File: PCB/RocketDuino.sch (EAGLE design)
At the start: 41 parts, among them J1 FTDI, Y1 16MHZ

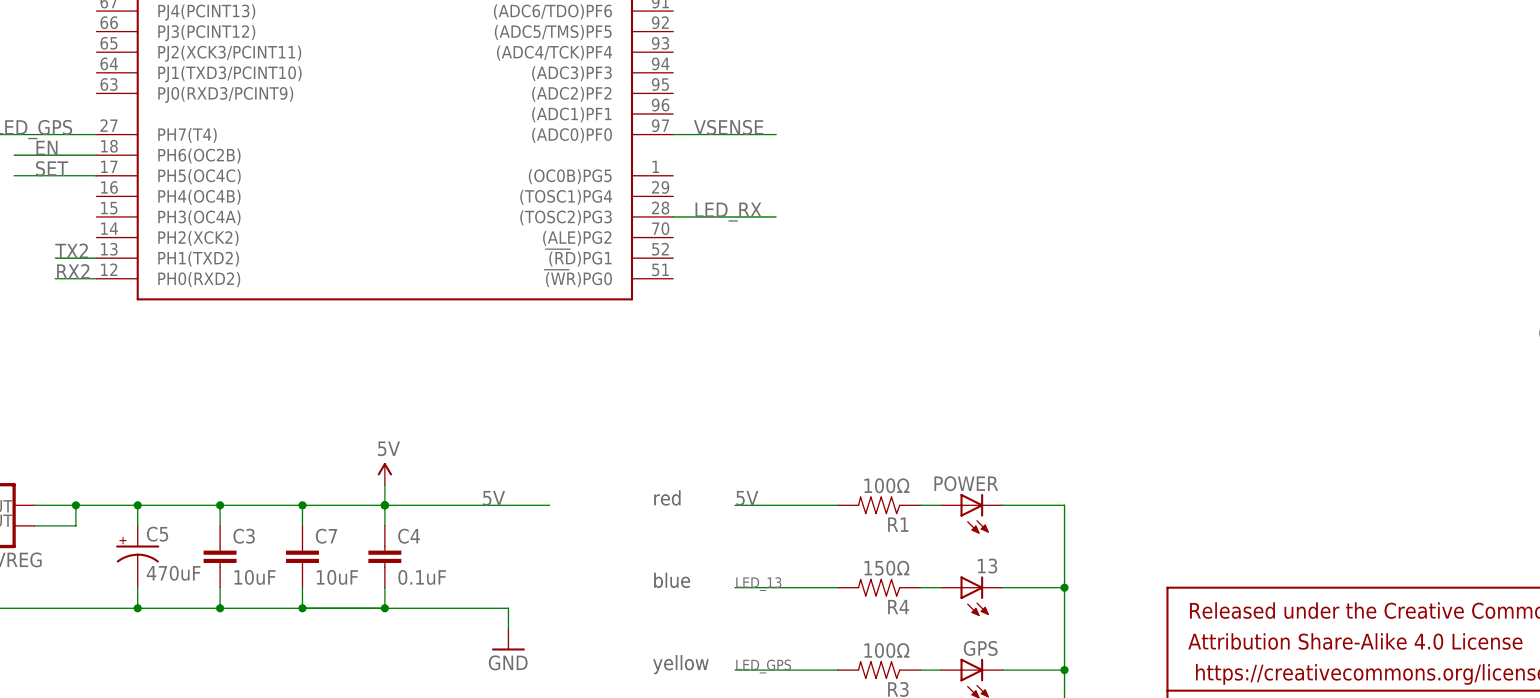
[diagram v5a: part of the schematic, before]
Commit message: Made C4 Explosive
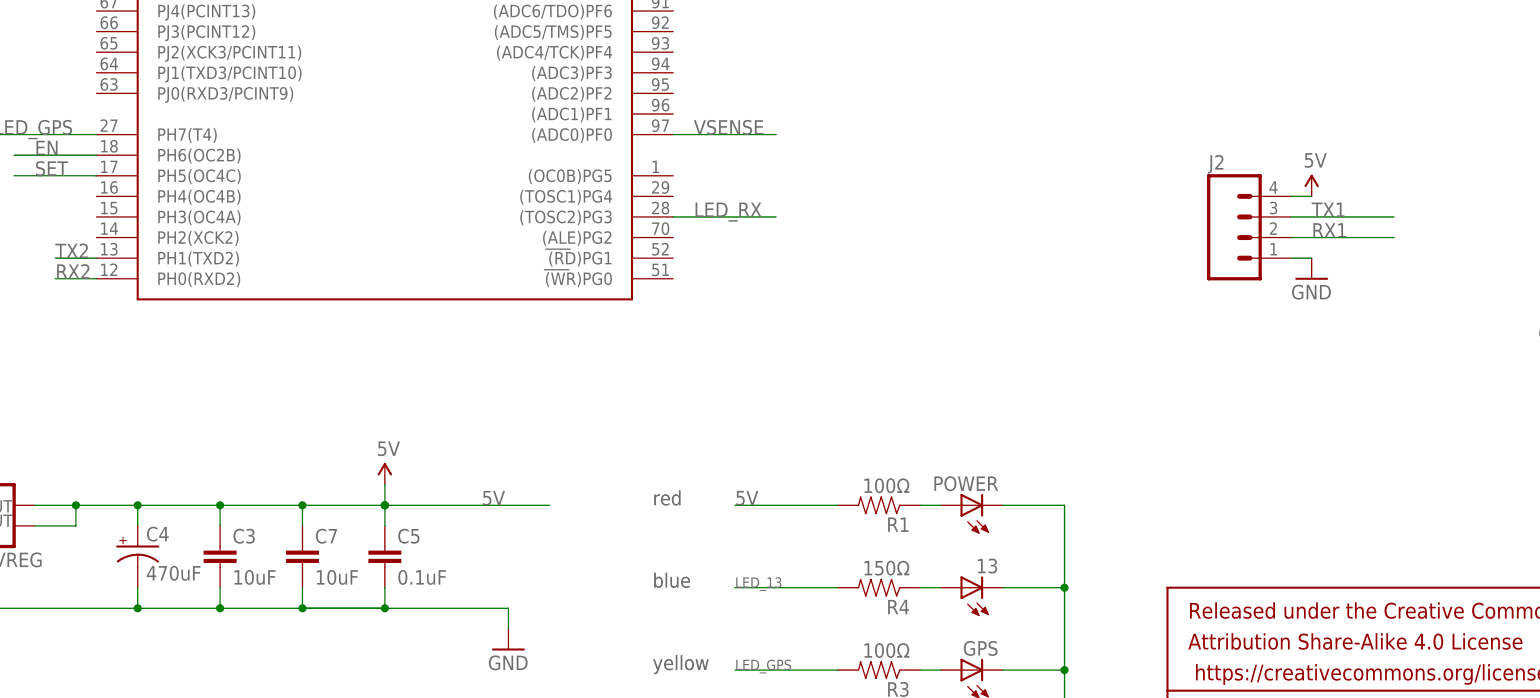
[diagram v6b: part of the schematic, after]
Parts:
- added J2: (no value), SparkFun-Connectors:M04POLAR
- C4: value 0.1uF -> 470uF; device SparkFun-Capacitors:CAP1206 -> SparkFun-Capacitors:CAP_POLPTH1
- C5: value 470uF -> 0.1uF; device SparkFun-Capacitors:CAP_POLPTH1 -> SparkFun-Capacitors:CAP1206
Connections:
- net 5V: now also C4.+, C5.1, J2.4; no longer C4.1, C5.+
- net GND: now also C4.-, C5.2, J2.1; no longer C4.2, C5.-
- net RX1: now also J2.2
- net TX1: now also J2.3
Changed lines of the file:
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@@
 <part name="SUPPLY5" library="SparkFun-Aesthetics" deviceset="5V" device=""/>
 <part name="C1" library="SparkFun-Capacitors" deviceset="CAP" device="1206" value="0.1uF"/>
-<part name="C4" library="SparkFun-Capacitors" deviceset="CAP" device="1206" value="0.1uF"/>
+<part name="C5" library="SparkFun-Capacitors" deviceset="CAP" device="1206" value="0.1uF"/>
 <part name="C2" library="SparkFun-Capacitors" deviceset="CAP" device="1206" value="10uF"/>
 <part name="C3" library="SparkFun-Capacitors" deviceset="CAP" device="1206" value="10uF"/>
@@
 <part name="CH_2" library="SparkFun-Connectors" deviceset="M02" device="LOCK_LONGPADS"/>
 <part name="VREG" library="SparkFun-PowerIC" deviceset="V_REG_LM1117" device="SOT223"/>
-<part name="C5" library="SparkFun-Capacitors" deviceset="CAP_POL" device="PTH1" value="470uF"/>
+<part name="C4" library="SparkFun-Capacitors" deviceset="CAP_POL" device="PTH1" value="470uF"/>
 <part name="Y1" library="SparkFun-FreqCtrl" deviceset="RESONATOR" device="16MHZ" value="16MHZ"/>
 <part name="R9" library="SparkFun-Resistors" deviceset="RESISTOR" device="1206" value="1MΩ"/>
@@
 <part name="MAIN" library="SparkFun-Connectors" deviceset="M02" device="LOCK_LONGPADS"/>
 <part name="C10" library="SparkFun-Capacitors" deviceset="CAP" device="1206" value="10uF"/>
+<part name="J2" library="SparkFun-Connectors" deviceset="M04" device="POLAR"/>
+<part name="SUPPLY8" library="SparkFun-Aesthetics" deviceset="5V" device=""/>
+<part name="GND16" library="SparkFun-Aesthetics" deviceset="GND" device=""/>
 </parts>
 <sheets>
@@
 <instance part="SUPPLY5" gate="G$1" x="114.3" y="43.18"/>
 <instance part="C1" gate="G$1" x="35.56" y="33.02"/>
-<instance part="C4" gate="G$1" x="114.3" y="33.02"/>
+<instance part="C5" gate="G$1" x="114.3" y="33.02"/>
 <instance part="C2" gate="G$1" x="45.72" y="33.02"/>
 <instance part="C3" gate="G$1" x="93.98" y="33.02"/>
@@
 <instance part="CH_2" gate="G$1" x="299.72" y="226.06" rot="R180"/>
 <instance part="VREG" gate="G$1" x="63.5" y="40.64"/>
-<instance part="C5" gate="G$1" x="83.82" y="35.56"/>
+<instance part="C4" gate="G$1" x="83.82" y="35.56"/>
 <instance part="Y1" gate="G$1" x="58.42" y="210.82" rot="R270"/>
 <instance part="R9" gate="G$1" x="38.1" y="210.82" rot="R90"/>
@@
 <instance part="MAIN" gate="G$1" x="17.78" y="36.83" rot="R180"/>
 <instance part="C10" gate="G$1" x="274.32" y="129.54"/>
+<instance part="J2" gate="G$1" x="220.98" y="73.66"/>
+<instance part="SUPPLY8" gate="G$1" x="228.6" y="78.74"/>
+<instance part="GND16" gate="1" x="228.6" y="68.58"/>
 </instances>
 <busses>
@@
 <wire x1="114.3" y1="30.48" x2="114.3" y2="27.94" width="0.1524" layer="91"/>
 <junction x="114.3" y="27.94"/>
-<pinref part="C4" gate="G$1" pin="2"/>
+<pinref part="C5" gate="G$1" pin="2"/>
 <pinref part="C3" gate="G$1" pin="2"/>
 <wire x1="114.3" y1="27.94" x2="104.14" y2="27.94" width="0.1524" layer="91"/>
@@
 <wire x1="83.82" y1="27.94" x2="93.98" y2="27.94" width="0.1524" layer="91"/>
 <wire x1="63.5" y1="33.02" x2="63.5" y2="27.94" width="0.1524" layer="91"/>
-<pinref part="C5" gate="G$1" pin="-"/>
+<pinref part="C4" gate="G$1" pin="-"/>
 <wire x1="83.82" y1="27.94" x2="83.82" y2="30.48" width="0.1524" layer="91"/>
 <junction x="83.82" y="27.94"/>
@@
 <pinref part="GND15" gate="1" pin="GND"/>
 <wire x1="292.1" y1="254" x2="289.56" y2="254" width="0.1524" layer="91"/>
+</segment>
+<segment>
+<pinref part="J2" gate="G$1" pin="1"/>
+<wire x1="226.06" y1="71.12" x2="228.6" y2="71.12" width="0.1524" layer="91"/>
+<pinref part="GND16" gate="1" pin="GND"/>
 </segment>
 </net>
@@
 <pinref part="SUPPLY5" gate="G$1" pin="5V"/>
 <junction x="93.98" y="40.64"/>
-<pinref part="C4" gate="G$1" pin="1"/>
+<pinref part="C5" gate="G$1" pin="1"/>
 <pinref part="C3" gate="G$1" pin="1"/>
 <label x="126.238" y="40.64" size="1.778" layer="95"/>
@@
 <wire x1="76.2" y1="38.1" x2="76.2" y2="40.64" width="0.1524" layer="91"/>
 <junction x="76.2" y="40.64"/>
-<pinref part="C5" gate="G$1" pin="+"/>
+<pinref part="C4" gate="G$1" pin="+"/>
 <wire x1="83.82" y1="40.64" x2="83.82" y2="38.1" width="0.1524" layer="91"/>
 <junction x="83.82" y="40.64"/>
@@
 <wire x1="266.7" y1="185.42" x2="269.24" y2="185.42" width="0.1524" layer="91"/>
 </segment>
+<segment>
+<pinref part="J2" gate="G$1" pin="4"/>
+<wire x1="226.06" y1="78.74" x2="228.6" y2="78.74" width="0.1524" layer="91"/>
+<pinref part="SUPPLY8" gate="G$1" pin="5V"/>
+</segment>
 </net>
 <net name="TX1" class="0">
@@
 <label x="226.06" y="193.04" size="1.778" layer="95"/>
 </segment>
+<segment>
+<pinref part="J2" gate="G$1" pin="3"/>
+<wire x1="226.06" y1="76.2" x2="238.76" y2="76.2" width="0.1524" layer="91"/>
+<label x="228.6" y="76.2" size="1.778" layer="95"/>
+</segment>
 </net>
 <net name="RX1" class="0">
@@
 <label x="226.06" y="190.5" size="1.778" layer="95"/>
 </segment>
-</net>
+<segment>
+<pinref part="J2" gate="G$1" pin="2"/>
+<wire x1="226.06" y1="73.66" x2="238.76" y2="73.66" width="0.1524" layer="91"/>
+<label x="228.6" y="73.66" size="1.778" layer="95"/>
+</segment>
+</net>

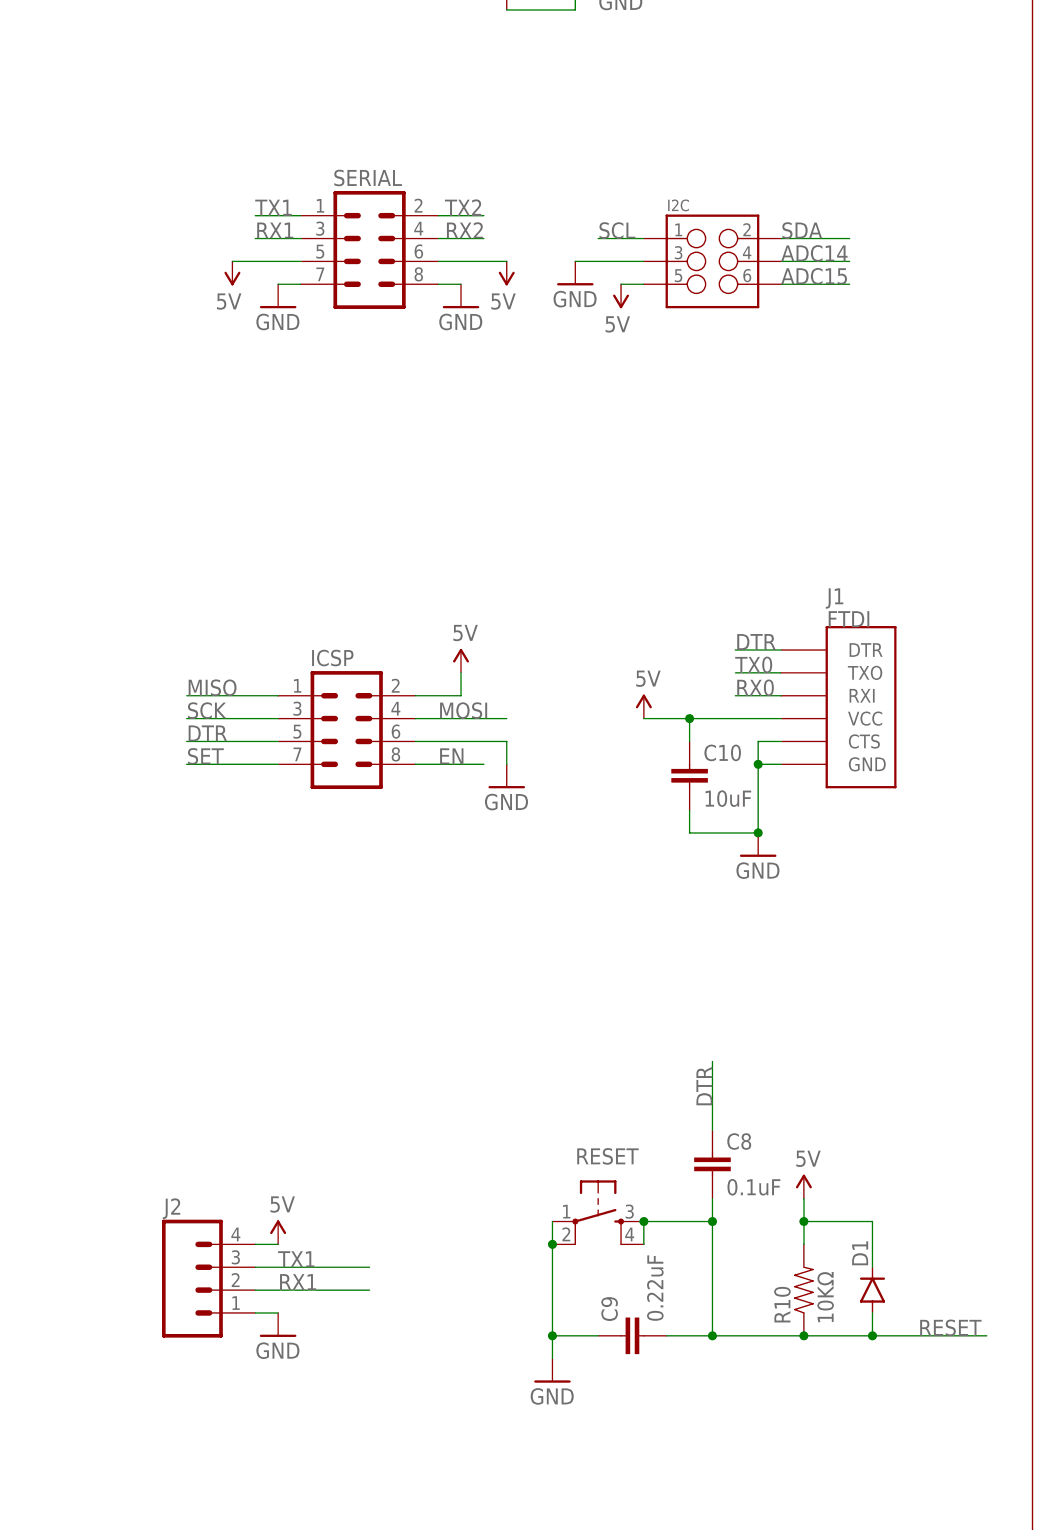
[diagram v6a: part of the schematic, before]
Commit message: Seperated Serial 1 & 2
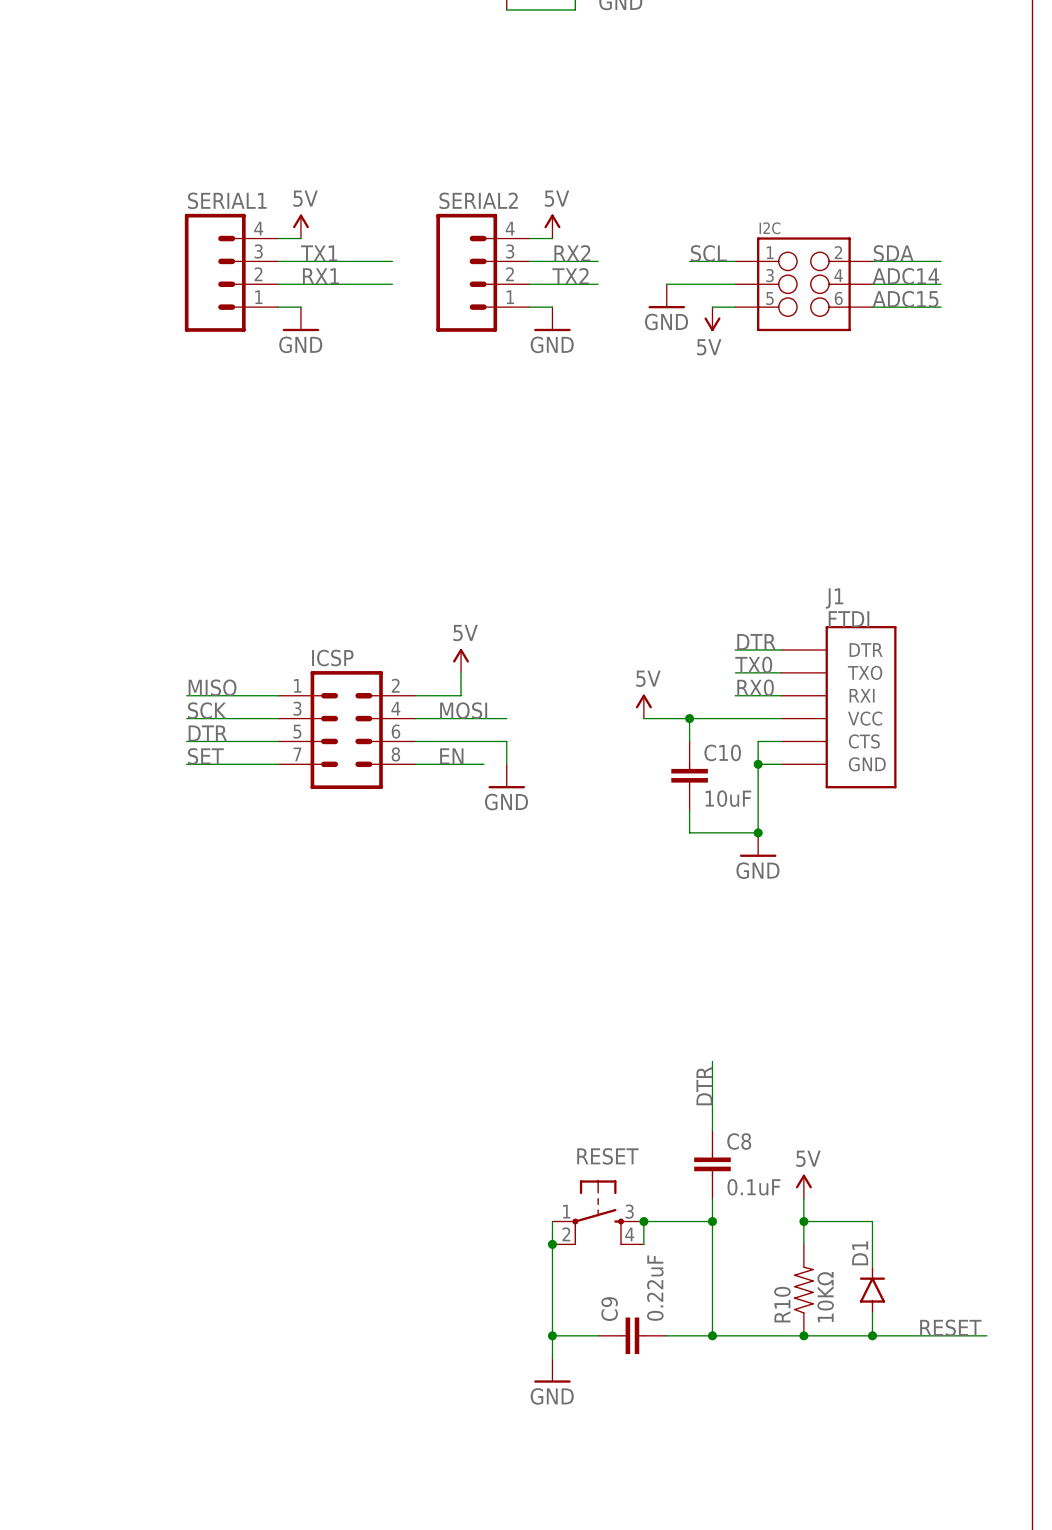
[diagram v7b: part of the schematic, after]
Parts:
- removed J2: (no value), SparkFun-Connectors:M04POLAR
- removed SERIAL: (no value), SparkFun-Connectors:M04X2
- added SERIAL1, SERIAL2: (no value), SparkFun-Connectors:M04POLAR
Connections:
- net 5V: now also SERIAL1.4, SERIAL2.4; no longer J2.4, SERIAL.5, SERIAL.6
- net GND: now also SERIAL1.1, SERIAL2.1; no longer J2.1, SERIAL.7, SERIAL.8
- net RX1: now also SERIAL1.2; no longer J2.2, SERIAL.3
- net RX2: now also SERIAL2.3; no longer SERIAL.4
- net TX1: now also SERIAL1.3; no longer J2.3, SERIAL.1
- net TX2: now also SERIAL2.2; no longer SERIAL.2
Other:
- moved on the sheet: I2C

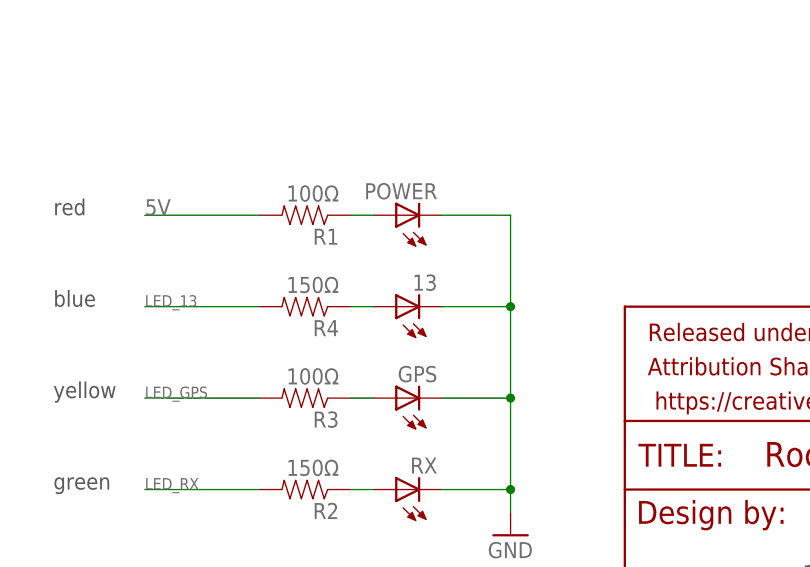
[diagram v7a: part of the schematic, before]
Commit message: Add Labels for Serial
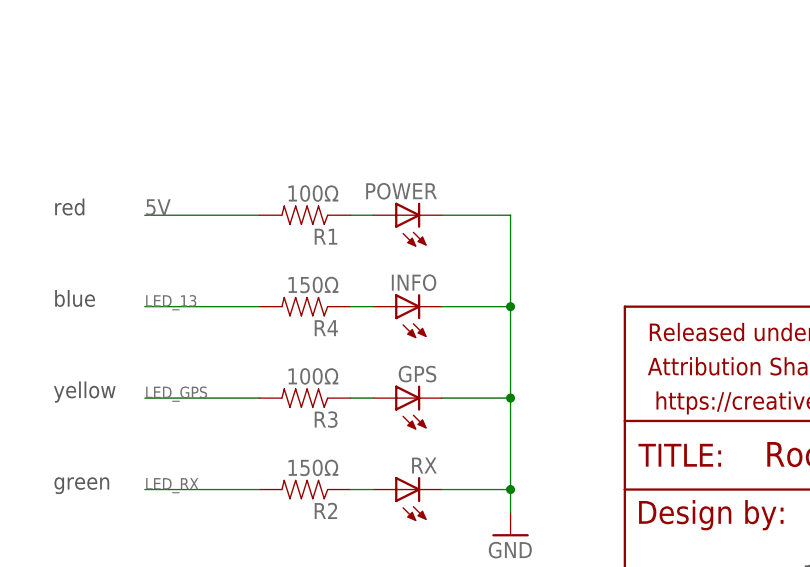
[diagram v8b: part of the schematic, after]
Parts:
- renumbered 13 to INFO
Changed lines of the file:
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@@
 <part name="LOGO1" library="SparkFun-Aesthetics" deviceset="OSHW-LOGO" device="M" value="OSHW-LOGOM"/>
 <part name="GND5" library="SparkFun-Aesthetics" deviceset="GND" device=""/>
-<part name="13" library="led" deviceset="LED" device="SML0805"/>
+<part name="INFO" library="led" deviceset="LED" device="SML0805"/>
 <part name="MOS" library="SparkFun-Connectors" deviceset="M02" device="LOCK_LONGPADS"/>
 <part name="SUPPLY1" library="SparkFun-Aesthetics" deviceset="5V" device=""/>
@@
 <instance part="LOGO1" gate="G$1" x="187.96" y="248.92"/>
 <instance part="GND5" gate="1" x="281.94" y="121.92"/>
-<instance part="13" gate="G$1" x="185.42" y="30.48" rot="R90"/>
+<instance part="INFO" gate="G$1" x="185.42" y="30.48" rot="R90"/>
 <instance part="MOS" gate="G$1" x="299.72" y="256.54" rot="R180"/>
 <instance part="SUPPLY1" gate="G$1" x="68.58" y="200.66"/>
@@
 </segment>
 <segment>
-<pinref part="13" gate="G$1" pin="C"/>
+<pinref part="INFO" gate="G$1" pin="C"/>
 <wire x1="198.12" y1="30.48" x2="190.5" y2="30.48" width="0.1524" layer="91"/>
 <pinref part="POWER" gate="G$1" pin="C"/>
@@
 <net name="N$3" class="0">
 <segment>
-<pinref part="13" gate="G$1" pin="A"/>
+<pinref part="INFO" gate="G$1" pin="A"/>
 <wire x1="180.34" y1="30.48" x2="182.88" y2="30.48" width="0.1524" layer="91"/>
 <pinref part="R4" gate="G$1" pin="1"/>
